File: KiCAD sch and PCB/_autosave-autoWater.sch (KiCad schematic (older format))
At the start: 23 parts, among them J1 Li-ion 18650, J2 PROG, J3 Water Pump, J4 Soil Humidity Sensor, Q1 AO3400, Q2 AO3400, SW1 SW_Push_Dual, U1 ATtiny13-20SSU

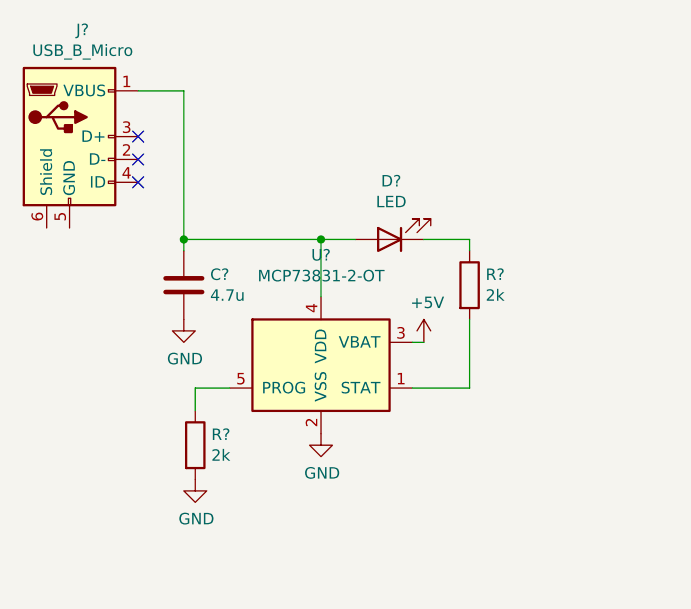
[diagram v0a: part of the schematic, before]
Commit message: added li ion charger on pcb
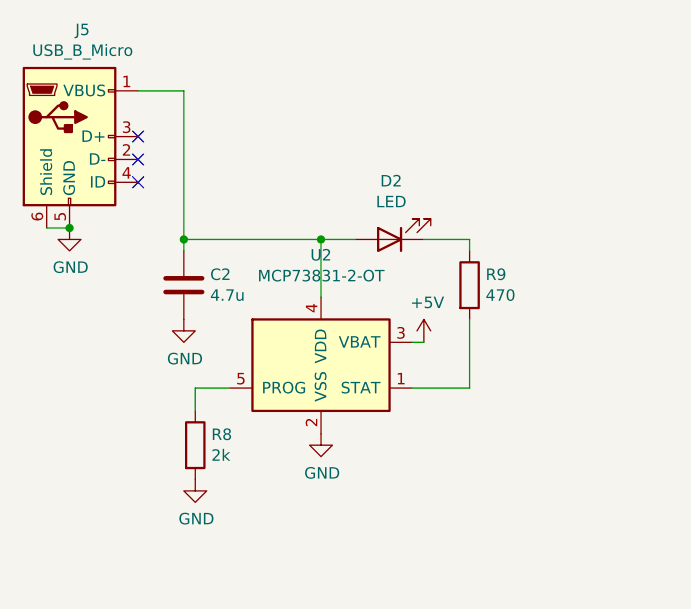
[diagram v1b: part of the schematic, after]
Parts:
- C2: renamed from C?; footprint (none) -> Capacitor_SMD:C_0805_2012Metric_Pad1.15x1.40mm_HandSolder
- D2: renamed from D?; footprint (none) -> LED_SMD:LED_0805_2012Metric_Pad1.15x1.40mm_HandSolder
- J5: renamed from J?; footprint (none) -> Connector_USB:USB_Micro-B_Wuerth_629105150521
- R8: renamed from R?; footprint (none) -> Resistor_SMD:R_0805_2012Metric_Pad1.15x1.40mm_HandSolder
- R9: renamed from R?; value 2k -> 470; footprint (none) -> Resistor_SMD:R_0805_2012Metric_Pad1.15x1.40mm_HandSolder
- gave numbers to parts that had none: 1
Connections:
- net GND: now also J5.5 (GND), J5.6 (Shield)
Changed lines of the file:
@@
 Connection ~ 8800 5200
 $Comp
-L Connector:USB_B_Micro J?
+L Connector:USB_B_Micro J5
 U 1 1 5ED77C14
 P 1000 1150
-F 0 "J?" H 1057 1617 50  0000 C CNN
+F 0 "J5" H 1057 1617 50  0000 C CNN
 F 1 "USB_B_Micro" H 1057 1526 50  0000 C CNN
-F 2 "" H 1150 1100 50  0001 C CNN
+F 2 "Connector_USB:USB_Micro-B_Wuerth_629105150521" H 1150 1100 50  0001 C CNN
 F 3 "~" H 1150 1100 50  0001 C CNN
 	1    1000 1150
@@
 NoConn ~ 1300 1350
 $Comp
-L Device:R R?
+L Device:R R8
 U 1 1 5ED7E586
 P 1550 2500
-F 0 "R?" H 1620 2546 50  0000 L CNN
+F 0 "R8" H 1620 2546 50  0000 L CNN
 F 1 "2k" H 1620 2455 50  0000 L CNN
-F 2 "" V 1480 2500 50  0001 C CNN
+F 2 "Resistor_SMD:R_0805_2012Metric_Pad1.15x1.40mm_HandSolder" V 1480 2500 50  0001 C CNN
 F 3 "~" H 1550 2500 50  0001 C CNN
 	1    1550 2500
@@
 $EndComp
 $Comp
-L Battery_Management:MCP73831-2-OT U?
+L Battery_Management:MCP73831-2-OT U2
 U 1 1 5ED87504
 P 2100 2150
-F 0 "U?" H 2100 2631 50  0000 C CNN
+F 0 "U2" H 2100 2631 50  0000 C CNN
 F 1 "MCP73831-2-OT" H 2100 2540 50  0000 C CNN
 F 2 "Package_TO_SOT_SMD:SOT-23-5" H 2150 1900 50  0001 L CIN
@@
 	1550 2250 1550 2350
 $Comp
-L power:GND #PWR?
+L power:GND #PWR02
 U 1 1 5ED80F71
 P 1550 2650
-F 0 "#PWR?" H 1550 2400 50  0001 C CNN
+F 0 "#PWR02" H 1550 2400 50  0001 C CNN
 F 1 "GND" H 1555 2477 50  0000 C CNN
 F 2 "" H 1550 2650 50  0001 C CNN
@@
 $EndComp
 $Comp
-L power:GND #PWR?
+L power:GND #PWR03
 U 1 1 5ED8174D
 P 2100 2450
-F 0 "#PWR?" H 2100 2200 50  0001 C CNN
+F 0 "#PWR03" H 2100 2200 50  0001 C CNN
 F 1 "GND" H 2105 2277 50  0000 C CNN
 F 2 "" H 2100 2450 50  0001 C CNN
@@
 $EndComp
 $Comp
-L Device:LED D?
+L Device:LED D2
 U 1 1 5ED81BE4
 P 2400 1600
-F 0 "D?" H 2393 1345 50  0000 C CNN
+F 0 "D2" H 2393 1345 50  0000 C CNN
 F 1 "LED" H 2393 1436 50  0000 C CNN
-F 2 "" H 2400 1600 50  0001 C CNN
+F 2 "LED_SMD:LED_0805_2012Metric_Pad1.15x1.40mm_HandSolder" H 2400 1600 50  0001 C CNN
 F 3 "~" H 2400 1600 50  0001 C CNN
 	1    2400 1600
@@
 $EndComp
 $Comp
-L Device:R R?
+L Device:R R9
 U 1 1 5ED82954
 P 2750 1800
-F 0 "R?" H 2820 1846 50  0000 L CNN
-F 1 "2k" H 2820 1755 50  0000 L CNN
-F 2 "" V 2680 1800 50  0001 C CNN
+F 0 "R9" H 2820 1846 50  0000 L CNN
+F 1 "470" H 2820 1755 50  0000 L CNN
+F 2 "Resistor_SMD:R_0805_2012Metric_Pad1.15x1.40mm_HandSolder" V 2680 1800 50  0001 C CNN
 F 3 "~" H 2750 1800 50  0001 C CNN
 	1    2750 1800
@@
 	2750 2250 2500 2250
 $Comp
-L Device:C C?
+L Device:C C2
 U 1 1 5ED885A2
 P 1500 1800
-F 0 "C?" H 1615 1846 50  0000 L CNN
+F 0 "C2" H 1615 1846 50  0000 L CNN
 F 1 "4.7u" H 1615 1755 50  0000 L CNN
-F 2 "" H 1538 1650 50  0001 C CNN
+F 2 "Capacitor_SMD:C_0805_2012Metric_Pad1.15x1.40mm_HandSolder" H 1538 1650 50  0001 C CNN
 F 3 "~" H 1500 1800 50  0001 C CNN
 	1    1500 1800
@@
 Connection ~ 1500 1600
 $Comp
-L power:GND #PWR?
+L power:GND #PWR01
 U 1 1 5ED90F67
 P 1500 1950
-F 0 "#PWR?" H 1500 1700 50  0001 C CNN
+F 0 "#PWR01" H 1500 1700 50  0001 C CNN
 F 1 "GND" H 1505 1777 50  0000 C CNN
 F 2 "" H 1500 1950 50  0001 C CNN
@@
 $EndComp
 $Comp
-L power:+5V #PWR?
+L power:+5V #PWR04
 U 1 1 5ED912FB
 P 2550 2050
-F 0 "#PWR?" H 2550 1900 50  0001 C CNN
+F 0 "#PWR04" H 2550 1900 50  0001 C CNN
 F 1 "+5V" H 2565 2223 50  0000 C CNN
 F 2 "" H 2550 2050 50  0001 C CNN
@@
 Wire Wire Line
 	2500 2050 2550 2050
+$Comp
+L power:GND #PWR0118
+U 1 1 5EDA0745
+P 1000 1550
+F 0 "#PWR0118" H 1000 1300 50  0001 C CNN
+F 1 "GND" H 1005 1377 50  0000 C CNN
+F 2 "" H 1000 1550 50  0001 C CNN
+F 3 "" H 1000 1550 50  0001 C CNN
+	1    1000 1550
+	1    0    0    -1
+$EndComp
+Wire Wire Line
+	900  1550 1000 1550
+Connection ~ 1000 1550
 $EndSCHEMATC
